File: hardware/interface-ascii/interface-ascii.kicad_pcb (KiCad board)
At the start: 2 copper layers, 88.9 x 132.1 mm, 51 parts, among them J1 Apple 2, J2 Apple 1, J3 UART, J4 Conn_01x05, J5 ISP header, J6 Keyboard, J7 SOL-20, SW1 Options, U1 ATmega328P, U2 74LS166, U3 74LS138, U4 74LS138, U5 74LS04

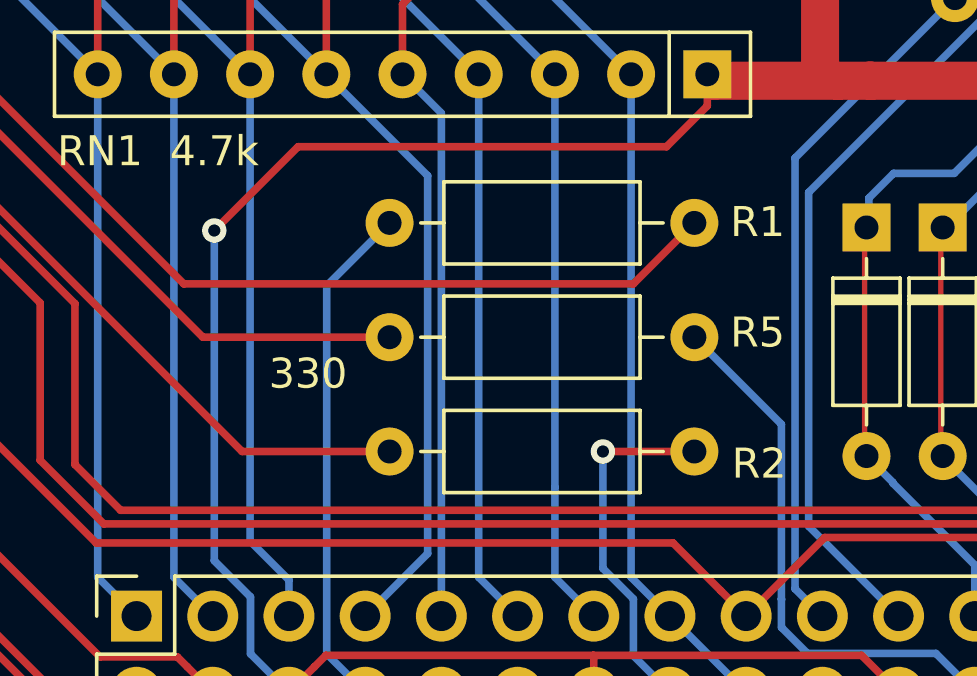
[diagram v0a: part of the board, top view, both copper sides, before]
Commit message: Move LED current limit resistors to keyboard PCB
For better matching of current limit resistors to LEDs, the resistors are moved
to the keyboard matrix PCB, where they can be tuned for maximum brightness (at
100% duty cycle).  This allows consistent keyboard brightness when a single
interface PCB is swapped between keyboard matrices.
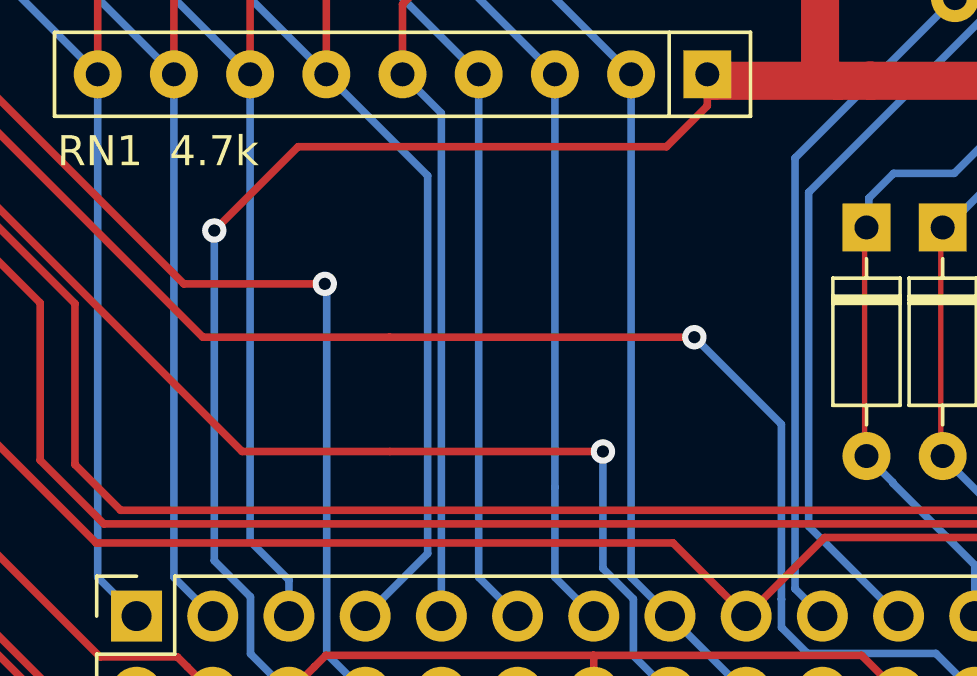
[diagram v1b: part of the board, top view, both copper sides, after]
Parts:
- removed R1, R2, R5: 330, Resistor_THT:R_Axial_DIN0207_L6.3mm_D2.5mm_P10.16mm_Horizontal
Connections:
- J6 pad 8: Net-(J6-Pad8) -> /LED1
- U5 pad 2: Net-(R5-Pad1) -> Net-(J6-Pad24)
- U5 pad 4: Net-(R2-Pad1) -> Net-(J6-Pad16)
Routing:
- net Net-(J6-Pad16): track 12.0 -> 130.4 mm, vias 1 -> 3
- net Net-(J6-Pad24): track 18.2 -> 132.7 mm, vias 0 -> 3
- net Net-(R2-Pad1): track 114.4 -> 0.00 mm, vias 2 -> 0
- net Net-(R5-Pad1): track 104.3 -> 0.00 mm, vias 2 -> 0
- net Net-(J6-Pad8): track 17.0 -> 0.00 mm
- net /LED1: track 101.1 -> 102.0 mm, vias 2 -> 3

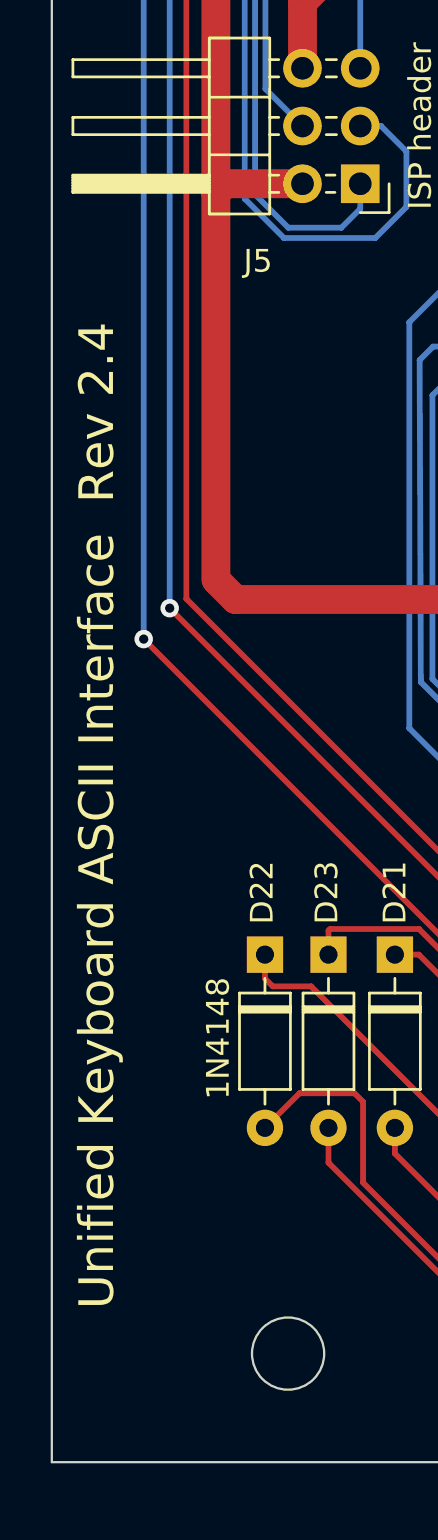
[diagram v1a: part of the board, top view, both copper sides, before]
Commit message: Cleanups, use cherry aligners with futaba keys, bump rev number
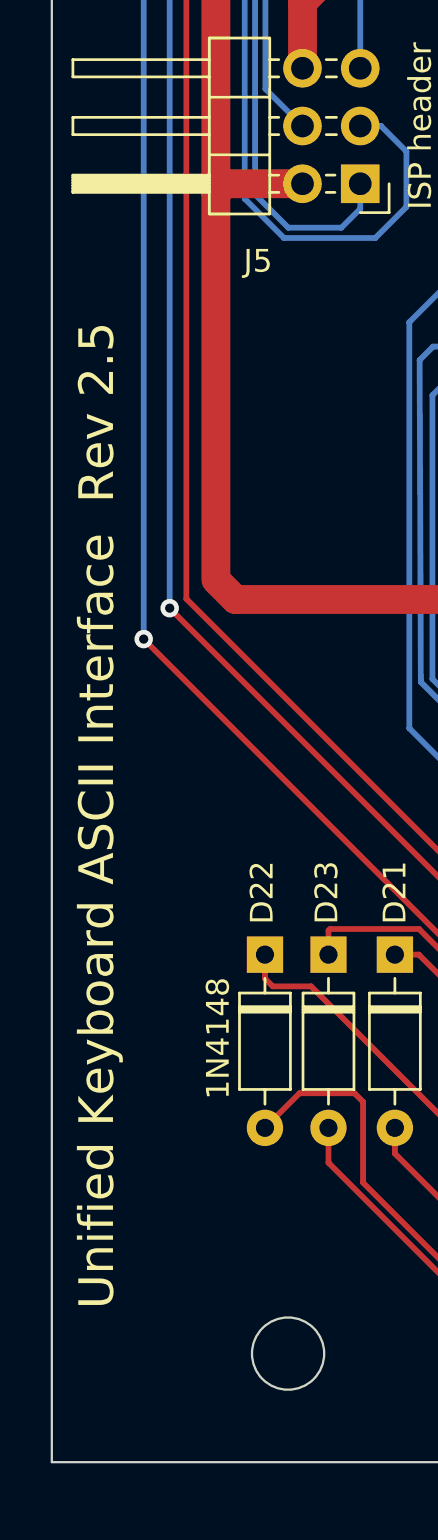
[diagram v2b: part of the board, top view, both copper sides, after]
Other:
- board text added: "Unified Keyboard ASCII Interface Rev 2.5"
- board text removed: "Unified Keyboard ASCII Interface Rev 2.4"
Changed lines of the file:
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@@
     (title "Unified Retro Keyboard")
     (date 2019-12-13)
-    (rev 2.4)
+    (rev 2.5)
   )
   (layers
@@
     (effects (font (size 1.524 1.524) (thickness 0.254)))
   )
-  (gr_text "Unified Keyboard ASCII Interface  Rev 2.4" (at 165.7374 155.0178 90) (layer B.SilkS)
+  (gr_text "Unified Keyboard ASCII Interface  Rev 2.5\n" (at 165.7374 155.0178 90) (layer B.SilkS)
     (effects (font (size 1.524 1.524) (thickness 0.254)) (justify mirror))
   )
-  (gr_text "Unified Keyboard ASCII Interface  Rev 2.4" (at 165.8136 154.4336 90) (layer F.SilkS)
+  (gr_text "Unified Keyboard ASCII Interface  Rev 2.5" (at 165.8136 154.4336 90) (layer F.SilkS)
     (effects (font (size 1.524 1.524) (thickness 0.254)))
   )
@@
   (segment (start 207.581838 174.271) (end 206.716201 173.405363) (width 0.254) (layer B.Cu) (net 86))
   (segment (start 211.8638 174.271) (end 207.581838 174.271) (width 0.254) (layer B.Cu) (net 86))
+  (via (at 169.014 145.315) (size 0.8128) (drill 0.4064) (layers F.Cu B.Cu) (net 86))
+  (segment (start 187.429 163.73) (end 169.014 145.315) (width 0.254) (layer F.Cu) (net 86))
+  (segment (start 193.652 163.73) (end 187.429 163.73) (width 0.254) (layer F.Cu) (net 86))
+  (segment (start 174.957601 97.207399) (end 175.364 96.801) (width 0.254) (layer B.Cu) (net 86))
+  (segment (start 169.014 103.151) (end 174.957601 97.207399) (width 0.254) (layer B.Cu) (net 86))
+  (segment (start 195.43 94.896) (end 193.525 96.801) (width 0.254) (layer F.Cu) (net 86))
+  (segment (start 169.014 145.315) (end 169.014 103.151) (width 0.254) (layer B.Cu) (net 86))
+  (segment (start 175.938736 96.801) (end 175.364 96.801) (width 0.254) (layer F.Cu) (net 86))
+  (segment (start 193.525 96.801) (end 175.938736 96.801) (width 0.254) (layer F.Cu) (net 86))
+  (via (at 175.364 96.801) (size 0.8128) (drill 0.4064) (layers F.Cu B.Cu) (net 86))
+  (via (at 203.812 163.73) (size 0.8128) (drill 0.4064) (layers F.Cu B.Cu) (net 86))
+  (segment (start 203.8755 163.73) (end 203.812 163.73) (width 0.254) (layer F.Cu) (net 86))
+  (segment (start 193.652 163.73) (end 203.812 163.73) (width 0.254) (layer F.Cu) (net 86))
   (via (at 200.764 167.54) (size 0.8128) (drill 0.4064) (layers F.Cu B.Cu) (net 87))
   (segment (start 201.78 172.453792) (end 200.764 171.437792) (width 0.254) (layer B.Cu) (net 87))
@@
   (segment (start 201.78 174.3472) (end 201.78 172.453792) (width 0.254) (layer B.Cu) (net 87))
   (segment (start 202.9992 175.5664) (end 201.78 174.3472) (width 0.254) (layer B.Cu) (net 87))
+  (segment (start 188.73567 167.54) (end 167.871 146.67533) (width 0.254) (layer F.Cu) (net 87))
+  (segment (start 193.652 167.54) (end 188.73567 167.54) (width 0.254) (layer F.Cu) (net 87))
+  (via (at 167.871 146.67533) (size 0.8128) (drill 0.4064) (layers F.Cu B.Cu) (net 87))
+  (via (at 172.824 97.562998) (size 0.8128) (drill 0.4064) (layers F.Cu B.Cu) (net 87))
+  (segment (start 173.398736 97.562998) (end 172.824 97.562998) (width 0.254) (layer F.Cu) (net 87))
+  (segment (start 167.871 102.515998) (end 172.417601 97.969397) (width 0.254) (layer B.Cu) (net 87))
+  (segment (start 172.417601 97.969397) (end 172.824 97.562998) (width 0.254) (layer B.Cu) (net 87))
+  (segment (start 167.871 146.67533) (end 167.871 102.515998) (width 0.254) (layer B.Cu) (net 87))
+  (segment (start 200.51 94.896) (end 197.843002 97.562998) (width 0.254) (layer F.Cu) (net 87))
+  (segment (start 197.843002 97.562998) (end 173.398736 97.562998) (width 0.254) (layer F.Cu) (net 87))
+  (segment (start 193.652 167.54) (end 200.764 167.54) (width 0.254) (layer F.Cu) (net 87))
   (segment (start 191.5565 174.2837) (end 191.5565 162.0155) (width 0.254) (layer B.Cu) (net 89))
   (segment (start 192.8392 175.5664) (end 191.5565 174.2837) (width 0.254) (layer B.Cu) (net 89))
@@
   (segment (start 186.794 161.952) (end 169.74741 144.90541) (width 0.254) (layer F.Cu) (net 89))
   (segment (start 169.74741 106.545136) (end 169.74741 105.9704) (width 0.254) (layer F.Cu) (net 89))
-  (segment (start 188.73567 167.54) (end 167.871 146.67533) (width 0.254) (layer F.Cu) (net 87))
-  (segment (start 193.652 167.54) (end 188.73567 167.54) (width 0.254) (layer F.Cu) (net 87))
-  (via (at 167.871 146.67533) (size 0.8128) (drill 0.4064) (layers F.Cu B.Cu) (net 87))
-  (via (at 172.824 97.562998) (size 0.8128) (drill 0.4064) (layers F.Cu B.Cu) (net 87))
-  (segment (start 173.398736 97.562998) (end 172.824 97.562998) (width 0.254) (layer F.Cu) (net 87))
-  (segment (start 167.871 102.515998) (end 172.417601 97.969397) (width 0.254) (layer B.Cu) (net 87))
-  (segment (start 172.417601 97.969397) (end 172.824 97.562998) (width 0.254) (layer B.Cu) (net 87))
-  (segment (start 167.871 146.67533) (end 167.871 102.515998) (width 0.254) (layer B.Cu) (net 87))
-  (segment (start 200.51 94.896) (end 197.843002 97.562998) (width 0.254) (layer F.Cu) (net 87))
-  (segment (start 197.843002 97.562998) (end 173.398736 97.562998) (width 0.254) (layer F.Cu) (net 87))
-  (via (at 169.014 145.315) (size 0.8128) (drill 0.4064) (layers F.Cu B.Cu) (net 86))
-  (segment (start 187.429 163.73) (end 169.014 145.315) (width 0.254) (layer F.Cu) (net 86))
-  (segment (start 193.652 163.73) (end 187.429 163.73) (width 0.254) (layer F.Cu) (net 86))
-  (segment (start 174.957601 97.207399) (end 175.364 96.801) (width 0.254) (layer B.Cu) (net 86))
-  (segment (start 169.014 103.151) (end 174.957601 97.207399) (width 0.254) (layer B.Cu) (net 86))
-  (segment (start 195.43 94.896) (end 193.525 96.801) (width 0.254) (layer F.Cu) (net 86))
-  (segment (start 169.014 145.315) (end 169.014 103.151) (width 0.254) (layer B.Cu) (net 86))
-  (segment (start 175.938736 96.801) (end 175.364 96.801) (width 0.254) (layer F.Cu) (net 86))
-  (segment (start 193.525 96.801) (end 175.938736 96.801) (width 0.254) (layer F.Cu) (net 86))
-  (via (at 175.364 96.801) (size 0.8128) (drill 0.4064) (layers F.Cu B.Cu) (net 86))
-  (via (at 203.812 163.73) (size 0.8128) (drill 0.4064) (layers F.Cu B.Cu) (net 86))
-  (segment (start 203.8755 163.73) (end 203.812 163.73) (width 0.254) (layer F.Cu) (net 86))
-  (segment (start 193.652 163.73) (end 203.812 163.73) (width 0.254) (layer F.Cu) (net 86))
-  (segment (start 193.652 167.54) (end 200.764 167.54) (width 0.254) (layer F.Cu) (net 87))
   (segment (start 186.794 161.952) (end 191.493 161.952) (width 0.254) (layer F.Cu) (net 89))
   (via (at 191.493 161.952) (size 0.8128) (drill 0.4064) (layers F.Cu B.Cu) (net 89))

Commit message: Changed resistor value from "R_US" to 470
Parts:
- R4: value R_US -> 470
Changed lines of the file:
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@@
       (effects (font (size 1 1) (thickness 0.15)))
     )
-    (fp_text value R_US (at 5.08 2.37 90) (layer F.Fab) hide
+    (fp_text value 470 (at 5.08 2.37 90) (layer F.Fab) hide
       (effects (font (size 1 1) (thickness 0.15)))
     )

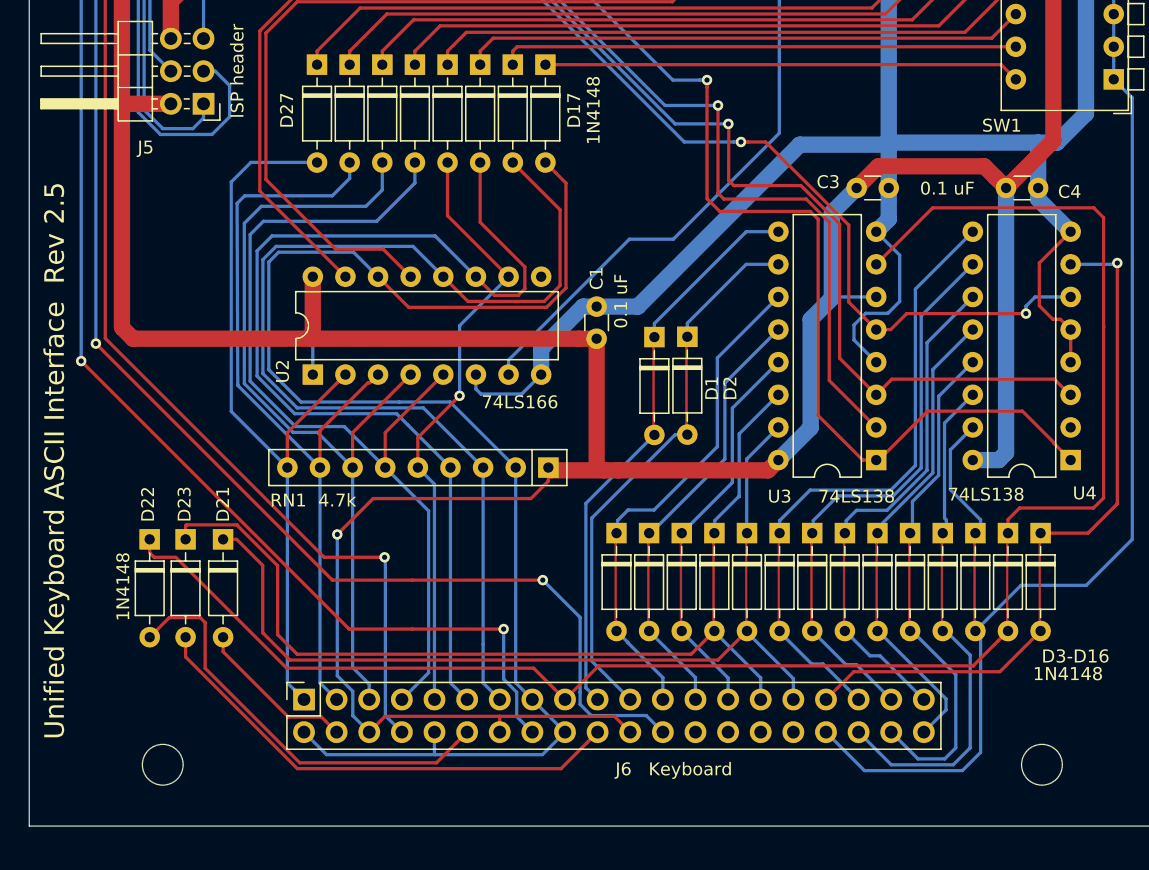
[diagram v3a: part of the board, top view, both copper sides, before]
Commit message: Fix unconnected wire to decoder for rows 8-15
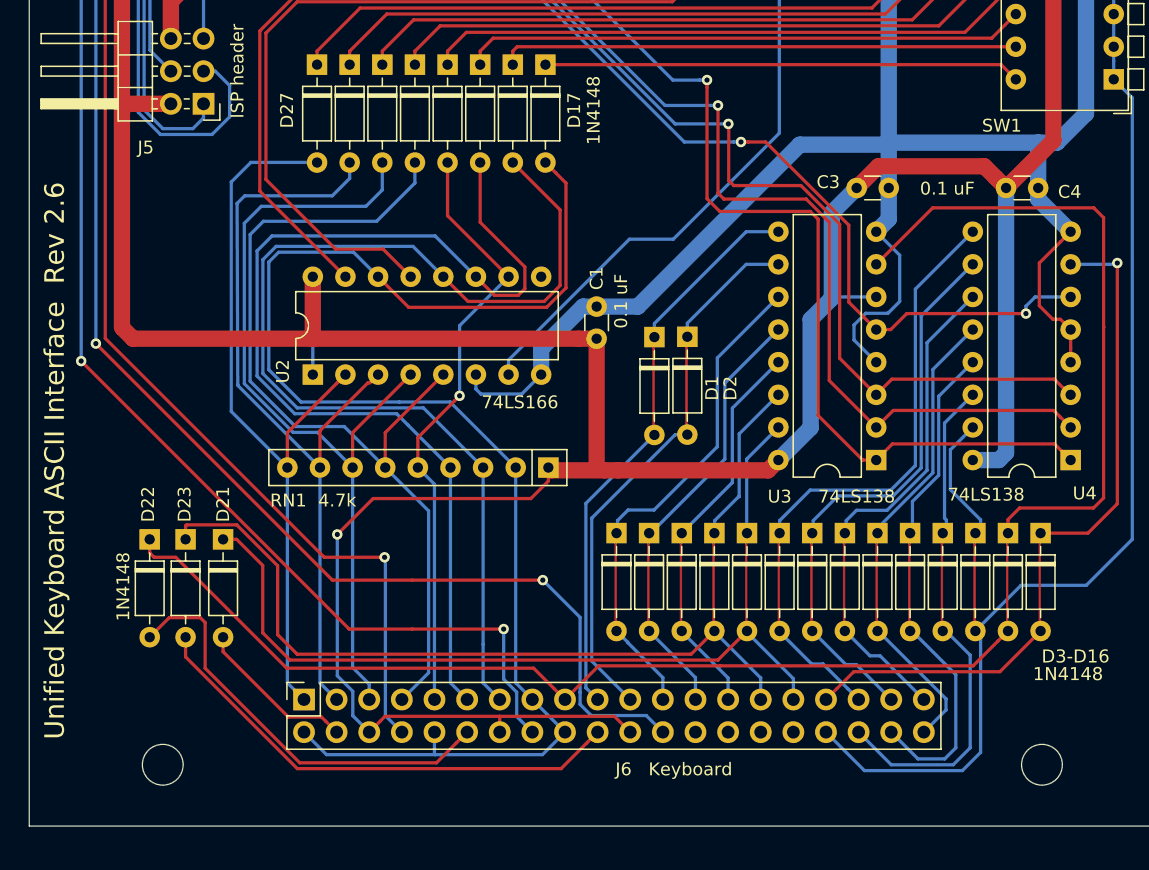
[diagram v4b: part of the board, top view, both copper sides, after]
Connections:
- U4 pad 2: Net-(U4-Pad2) -> Net-(U1-Pad24)
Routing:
- net Net-(U1-Pad24): track 66.4 -> 82.7 mm
- net Net-(U1-Pad23): track 86.5 -> 84.3 mm
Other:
- board text added: "Unified Keyboard ASCII Interface Rev 2.6"
- board text removed: "Unified Keyboard ASCII Interface Rev 2.5"
